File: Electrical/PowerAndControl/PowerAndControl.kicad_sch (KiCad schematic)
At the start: 26 parts, among them J1 Conn_02x03_Counter_Clockwise, SW2 SW_SPDT_312, U1 STC4054GR, U2 TPS22919QDCKRQ1, U3 TPS3840PL30DBVR

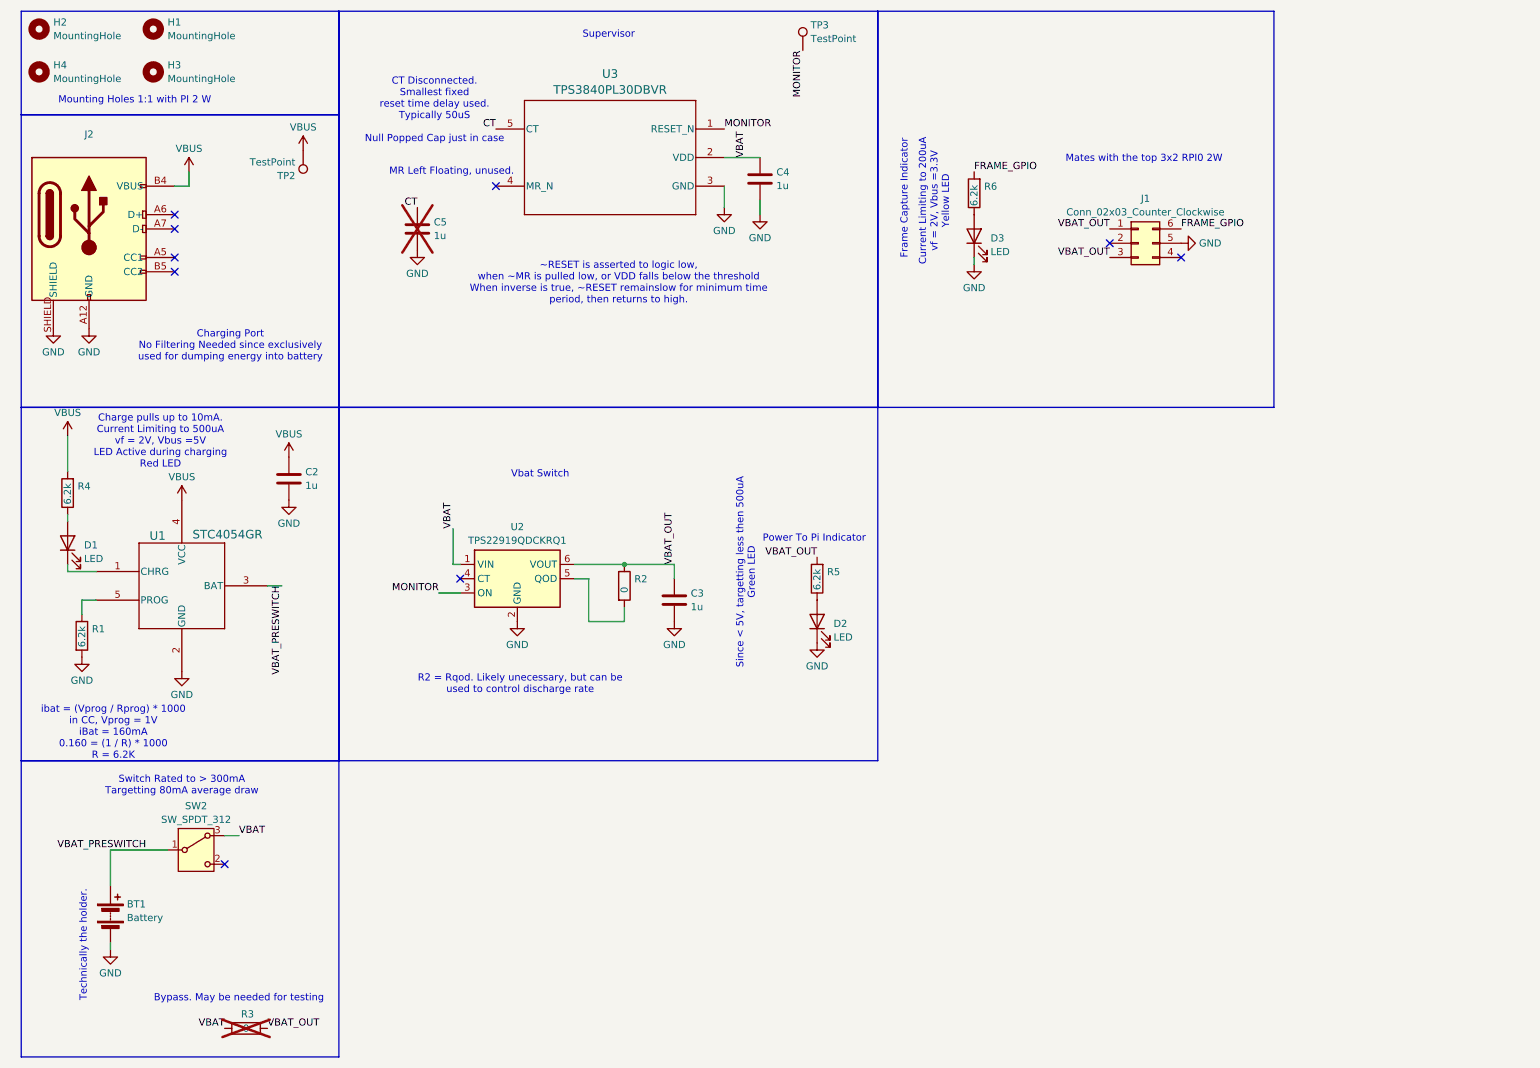
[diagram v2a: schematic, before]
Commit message: Rerouted Switch, Added Thermostat
Switch is now on the same side as the USB port. Should help
reduce z axis stackup.
Added thermostat, will shutoff if high temp
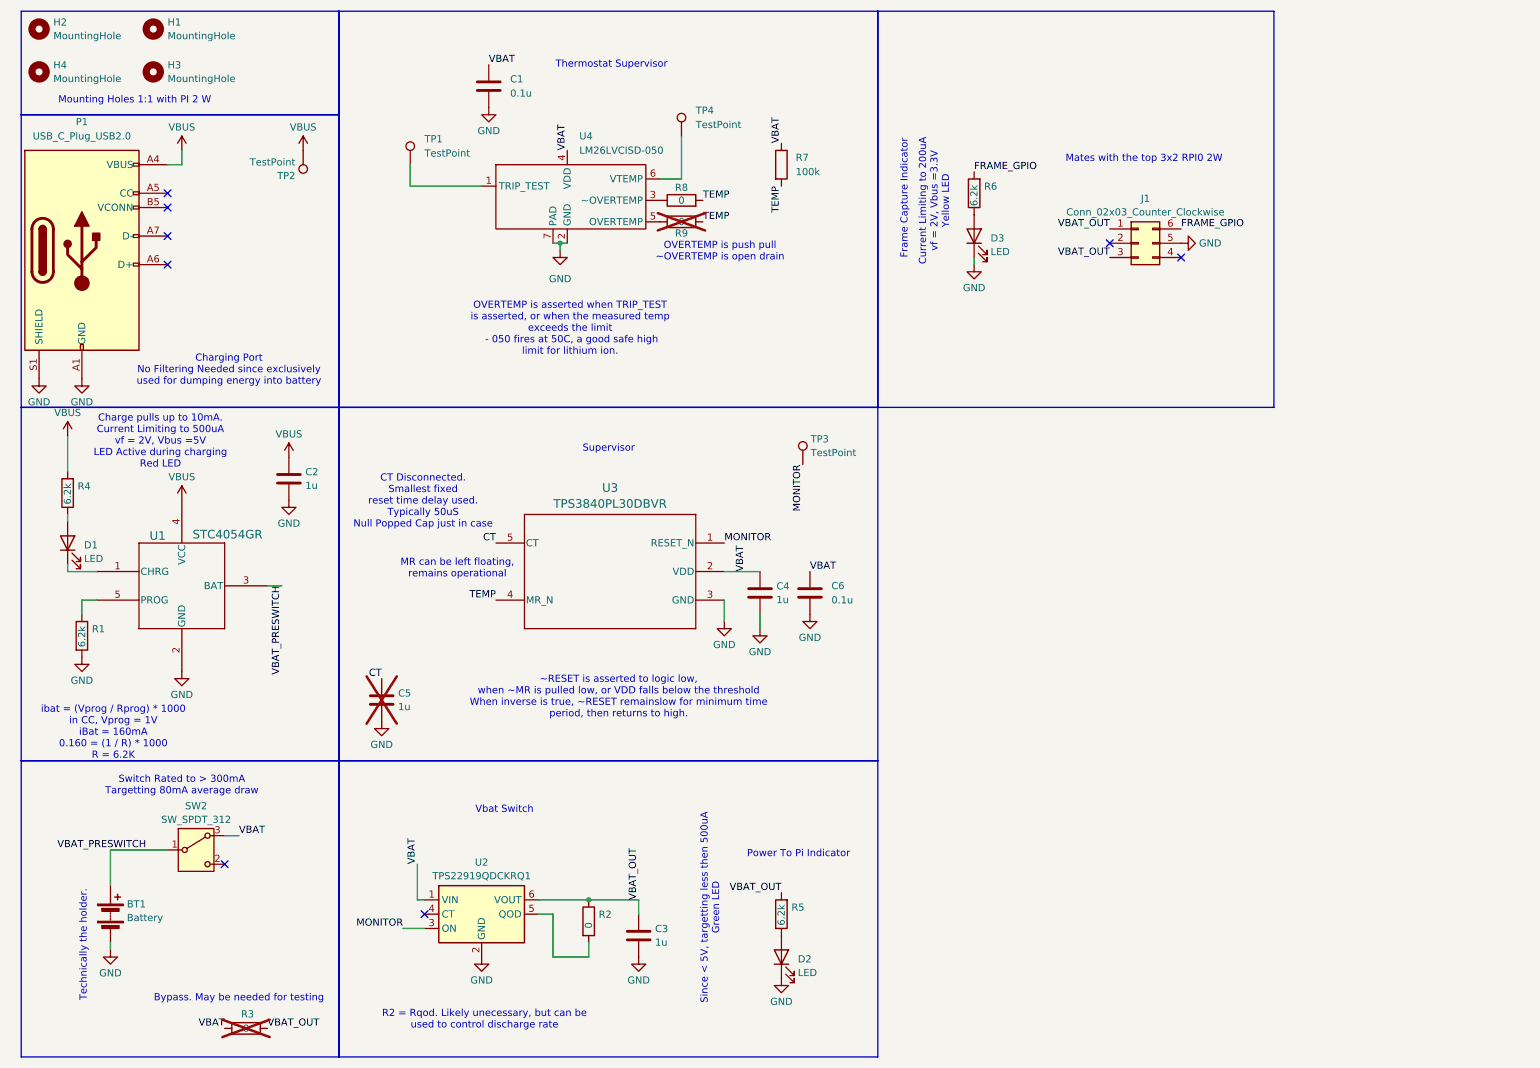
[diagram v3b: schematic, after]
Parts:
- removed J2: ~, Library:10176783-00011LF, symbol New_Library:USB_C_Receptacle_8P
- added C1, C6: 0.1u, Capacitor_SMD:C_0402_1005Metric_Pad0.74x0.62mm_HandSolder, symbol Device:C
- added P1: USB_C_Plug_USB2.0, Connector_USB:USB_C_Receptacle_GCT_USB4085, symbol Connector:USB_C_Plug_USB2.0
- added R7: 100k, symbol Device:R
- added R8, R9: 0, Resistor_SMD:R_0402_1005Metric_Pad0.72x0.64mm_HandSolder, symbol Device:R
- added TP1, TP4: TestPoint, TestPoint:TestPoint_Pad_1.0x1.0mm, symbol Connector:TestPoint
- added U4: LM26LVCISD-050, Package_SON:WSON-6-1EP_2x2mm_P0.65mm_EP1x1.6mm_ThermalVias, symbol New_Library:LM26LV
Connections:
- net GND: now also C1.2, C6.2, P1.A1 (GND), P1.A12 (GND), P1.B1 (GND), P1.B12 (GND), P1.S1 (SHIELD), U4.2 (GND), U4.7 (PAD)
- net VBAT: now also C1.1, C6.1, R7.1, U4.4 (VDD)
- net VBUS: now also P1.A4 (VBUS), P1.A9 (VBUS), P1.B4 (VBUS), P1.B9 (VBUS)
- net TEMP: now reaches U3.4 (MR_N)
- net TEMP: now also R7.2, R8.2, R9.2
- new net: TP1.1, U4.1 (TRIP_TEST)
- new net: R9.1, U4.5 (OVERTEMP)
- new net: TP4.1, U4.6 (VTEMP)
- new net: R8.1, U4.3 (~OVERTEMP)
- no-connect marks 9 -> 8
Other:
- note added: "MR can be left floating, remains operational"
- note added: "OVERTEMP is asserted when TRIP_TEST is asserted, or when the measured temp exceeds the limit - 050 fires at 50C, a good safe high limit for lithium ion."
- note added: "OVERTEMP is push pull ~OVERTEMP is open drain"
- note added: "Thermostat Supervisor"
- note removed: "MR Left Floating, unused."
- moved on the sheet: C3, C4, C5, D2, R2, R5, TP3, U2, U3

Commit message: Fixed up / Repositioned Model
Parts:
- R7: footprint (none) -> Resistor_SMD:R_0402_1005Metric_Pad0.72x0.64mm_HandSolder
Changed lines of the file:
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@@
 			)
 		)
-		(property "Footprint" ""
+		(property "Footprint" "Resistor_SMD:R_0402_1005Metric_Pad0.72x0.64mm_HandSolder"
 			(at 145.542 39.37 90)
 			(effects
